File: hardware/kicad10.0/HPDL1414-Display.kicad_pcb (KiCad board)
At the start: 2 copper layers, 55 x 22 mm, 10 parts, among them J1 Qwiic/Stemma QT, J2 Qwiic/Stemma QT, J3 SWDIO 3 Pin, U1 CH32V003AxMx

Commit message: kicad 10.0, drc passing
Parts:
- U1: footprint Package_SO:SOP-16_3.9x9.9mm_P1.27mm -> Package_SO:STC_SOP-16_3.9x9.9mm_P1.27mm
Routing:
- net VCC: track 67.1 -> 68.6 mm
- net WR1: track 42.3 -> 43.4 mm

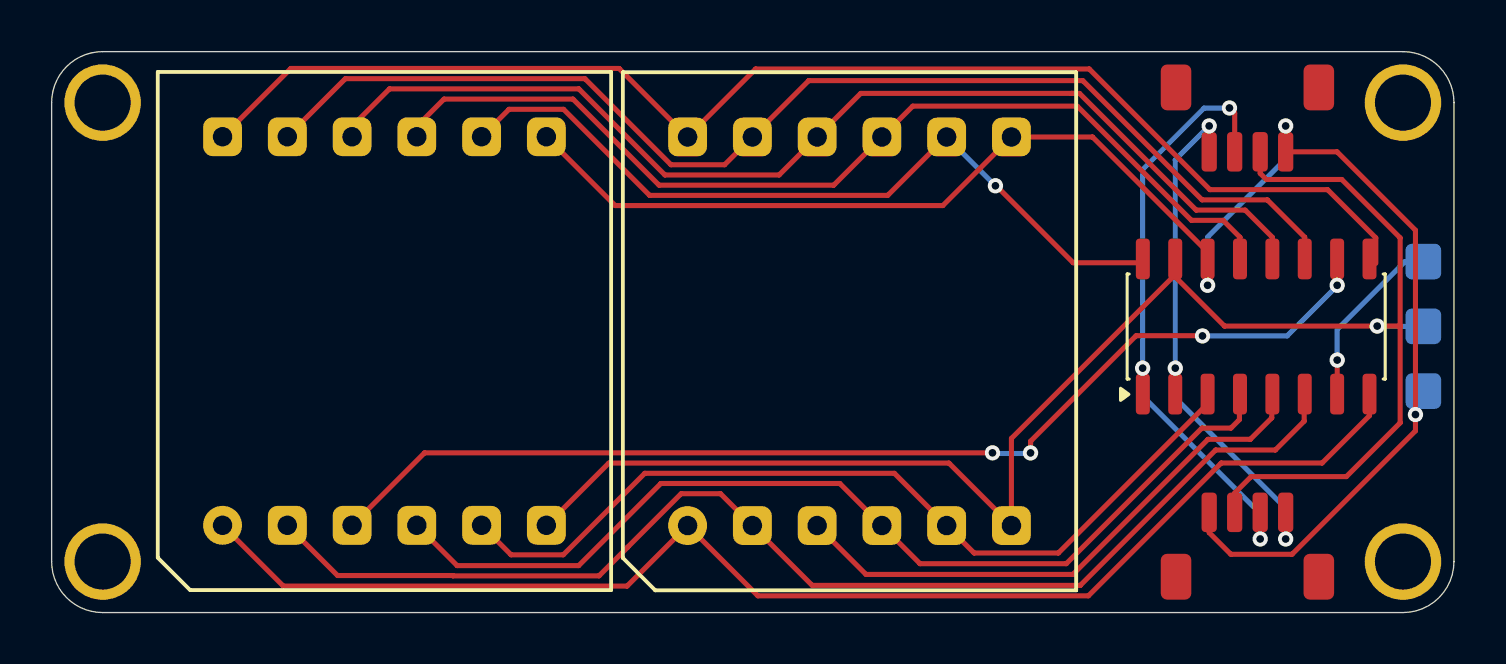
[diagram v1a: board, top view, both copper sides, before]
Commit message: cap and debug pads
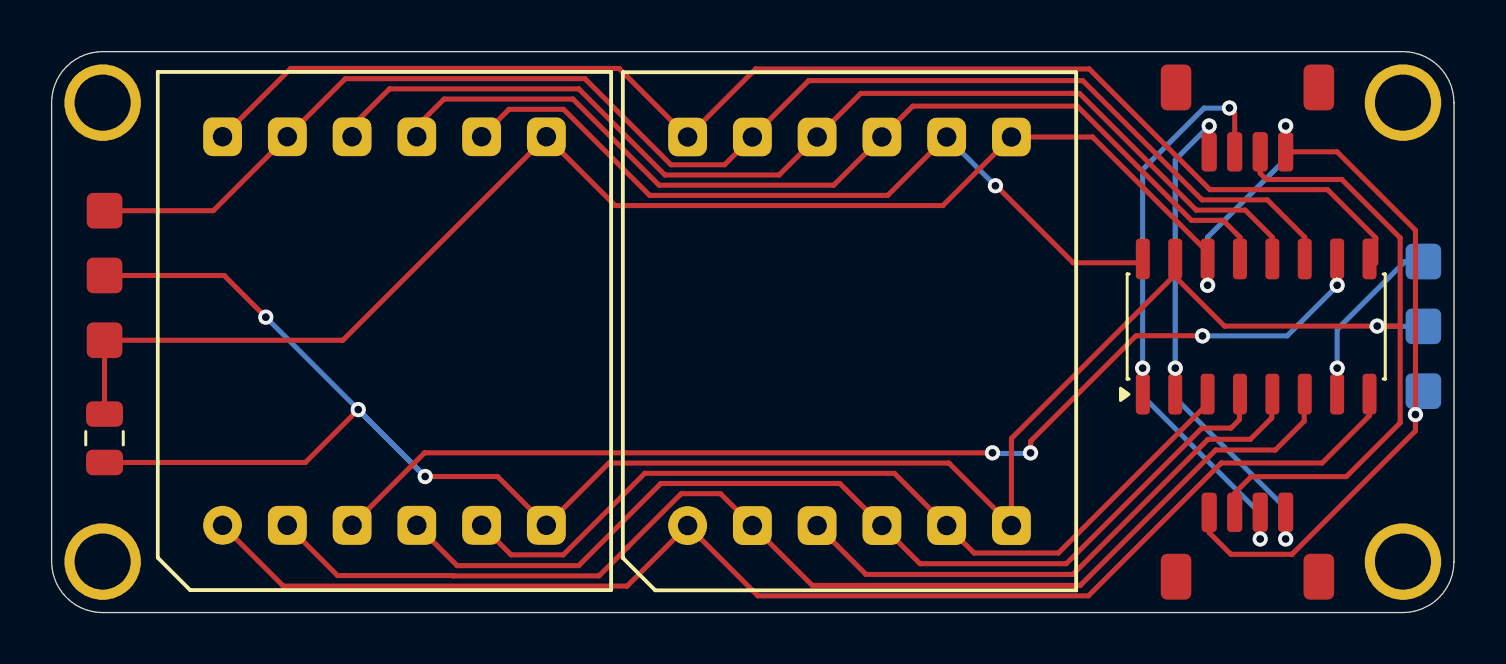
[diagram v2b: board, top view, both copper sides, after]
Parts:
- added C1: C, Capacitor_SMD:C_0805_2012Metric, F.Cu at (32.2, 45.2)
- added J4: 3 Pin, HPDL-1414:Pads_1x3_2.54mm, F.Cu at (32.2, 36.3)
- J3: value SWDIO 3 Pin -> 3 Pin
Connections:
- net D3 renamed D3/RST
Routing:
- net VCC: track 68.6 -> 104.5 mm, vias 1 -> 4
- net GND: track 63.8 -> 87.3 mm
- net D3/RST: track 47.2 -> 55.5 mm
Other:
- board text added: "2x HPDL-1414 I2C Display"

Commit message: adjustments
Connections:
- J3 pad 1: SWDIO -> VCC
- J3 pad 2: VCC -> GND
- J3 pad 3: GND -> SWDIO
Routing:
- net GND: track 87.3 -> 97.1 mm, vias 3 -> 2
- net SWDIO: track 6.86 -> 4.61 mm
- net VCC: track 104.5 -> 106.1 mm
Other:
- board text added: "rev 0.1"
